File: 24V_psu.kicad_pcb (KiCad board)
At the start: 2 copper layers, 92.5 x 45 mm, 27 parts, among them J1 AC_IN, J2 DC_OUT, Q1 TIP122, Q2 BC546B

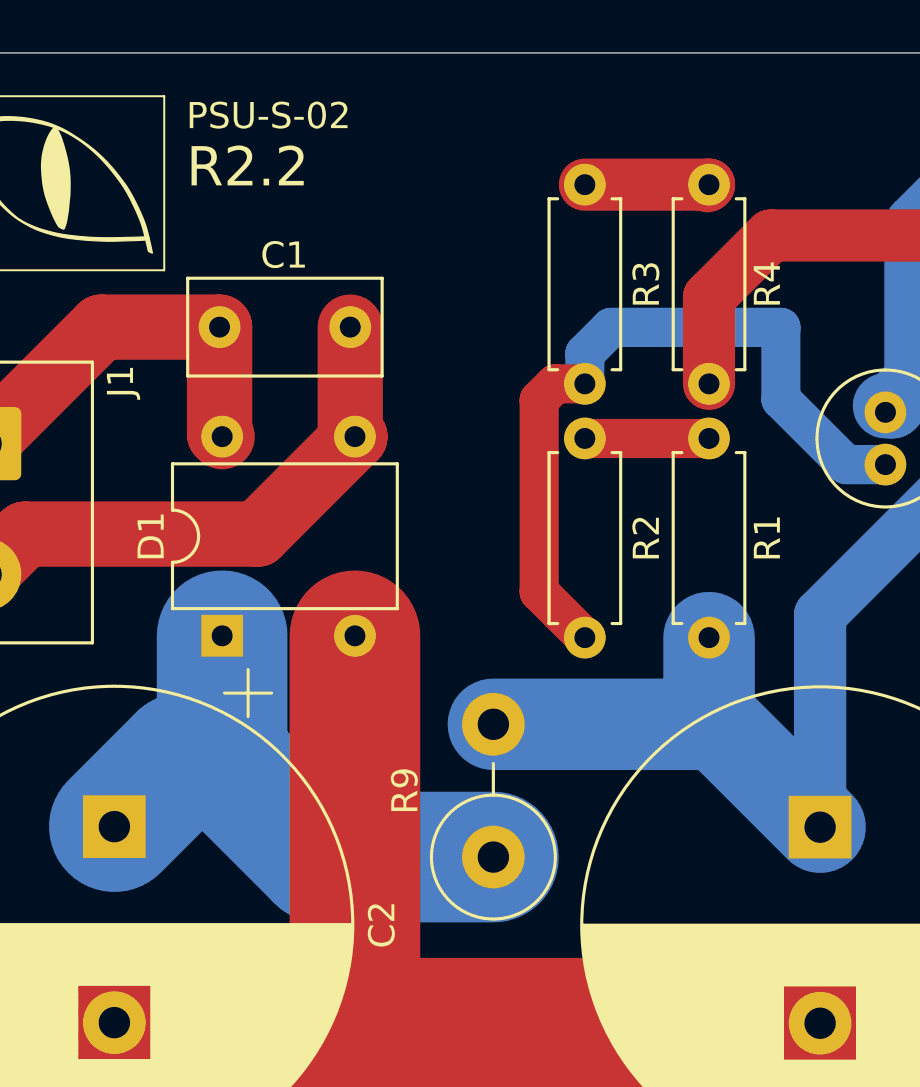
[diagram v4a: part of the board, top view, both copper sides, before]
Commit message: Rotate R9 around
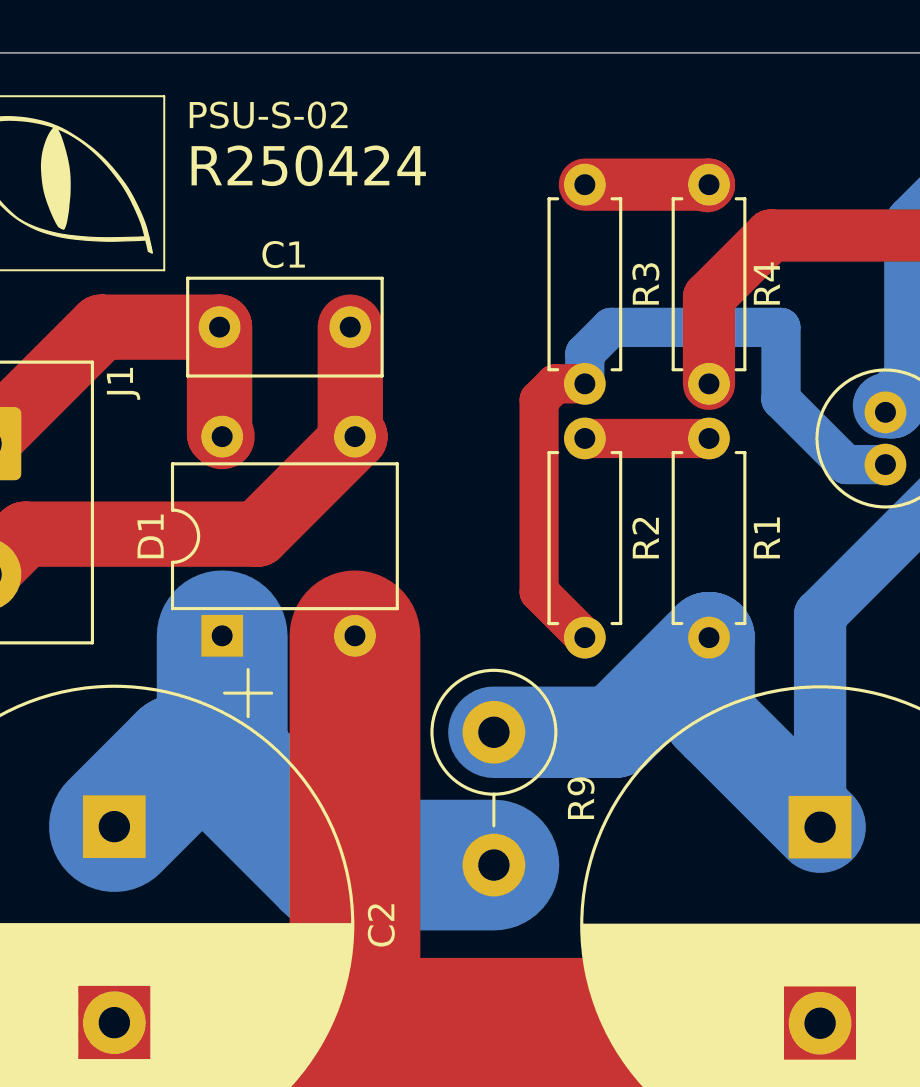
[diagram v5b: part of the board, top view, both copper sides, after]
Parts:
- moved R9 4.78 mm to (178.5, 73.5), turned to -90 degrees
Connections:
- R9 pad 1: Net-(D1-+) -> Net-(Q1-C)
- R9 pad 2: Net-(Q1-C) -> Net-(D1-+)
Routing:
- net Net-(Q1-C): track 44.7 -> 45.8 mm
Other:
- board text added: "R250424"
- board text removed: "R2.2"
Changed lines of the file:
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@@
 	(footprint "Resistor_THT:R_Axial_DIN0414_L11.9mm_D4.5mm_P5.08mm_Vertical"
 		(layer "F.Cu")
-		(at 178.5 78.265 90)
+		(at 178.52 73.49 -90)
 		(descr "Resistor, Axial_DIN0414 series, Axial, Vertical, pin pitch=5.08mm, 2W, length*diameter=11.9*4.5mm^2, http://www.vishay.com/docs/20128/wkxwrx.pdf")
 		(tags "Resistor Axial_DIN0414 series Axial Vertical pin pitch 5.08mm 2W length 11.9mm diameter 4.5mm")
@@
 		)
 		(property "Datasheet" ""
-			(at 0 0 90)
+			(at 0 0 270)
 			(unlocked yes)
 			(layer "F.Fab")
@@
 		)
 		(property "Description" "Resistor"
-			(at 0 0 90)
+			(at 0 0 270)
 			(unlocked yes)
 			(layer "F.Fab")
@@
 		)
 		(fp_line
-			(start 6.53 -2.5)
-			(end -2.5 -2.5)
+			(start -2.5 2.5)
+			(end 6.53 2.5)
 			(stroke
 				(width 0.05)
@@
 		)
 		(fp_line
-			(start -2.5 -2.5)
-			(end -2.5 2.5)
+			(start 6.53 2.5)
+			(end 6.53 -2.5)
 			(stroke
 				(width 0.05)
@@
 		)
 		(fp_line
-			(start 6.53 2.5)
-			(end 6.53 -2.5)
+			(start -2.5 -2.5)
+			(end -2.5 2.5)
 			(stroke
 				(width 0.05)
@@
 		)
 		(fp_line
-			(start -2.5 2.5)
-			(end 6.53 2.5)
+			(start 6.53 -2.5)
+			(end -2.5 -2.5)
 			(stroke
 				(width 0.05)
@@
 		)
 		(pad "1" thru_hole circle
-			(at 0 0 90)
+			(at 0 0 270)
 			(size 2.4 2.4)
 			(drill 1.2)
 			(layers "*.Cu" "*.Mask")
 			(remove_unused_layers no)
-			(net 3 "Net-(D1-+)")
+			(net 13 "Net-(Q1-C)")
 			(pintype "passive")
 		)
 		(pad "2" thru_hole oval
-			(at 5.08 0 90)
+			(at 5.08 0 270)
 			(size 2.4 2.4)
 			(drill 1.2)
 			(layers "*.Cu" "*.Mask")
 			(remove_unused_layers no)
-			(net 13 "Net-(Q1-C)")
+			(net 3 "Net-(D1-+)")
 			(pintype "passive")
 		)
@@
 		)
 	)
-	(gr_text "R2.2"
+	(gr_text "R250424"
 		(at 166.75 52.75 0)
 		(layer "F.SilkS")
@@
 	)
 	(segment
-		(start 171.891156 78.265)
-		(end 178.5 78.265)
+		(start 168.124188 74.498032)
+		(end 172.196156 78.57)
 		(width 5)
 		(layer "B.Cu")
@@
 	)
 	(segment
-		(start 168.124188 74.498032)
-		(end 166.601968 74.498032)
+		(start 172.196156 78.57)
+		(end 178.52 78.57)
 		(width 5)
 		(layer "B.Cu")
@@
 	(segment
 		(start 168.124188 74.498032)
-		(end 171.891156 78.265)
+		(end 166.601968 74.498032)
 		(width 5)
 		(layer "B.Cu")
@@
 	)
 	(segment
+		(start 183.13 73.49)
+		(end 178.52 73.49)
+		(width 3.5)
+		(layer "B.Cu")
+		(net 13)
+	)
+	(segment
 		(start 191 77.12222)
 		(end 191 69)
@@
 	)
 	(segment
-		(start 178.5 73.185)
-		(end 187.06278 73.185)
+		(start 187.06278 73.185)
+		(end 191 77.12222)
 		(width 3.5)
 		(layer "B.Cu")
@@
 	)
 	(segment
-		(start 187.06278 73.185)
-		(end 191 77.12222)
+		(start 186.75 69.87)
+		(end 183.13 73.49)
 		(width 3.5)
 		(layer "B.Cu")
@@
 	)
 	(group ""
-		(members "e9ad10b2-7d5c-4e9c-9937-1661a8a48dcf" "f2c60f9c-6234-4306-9854-33b4cfb3092c"
-			"fc57d3f7-0cdc-4cbc-a943-f06b294e3fd0"
-		)
-	)
-	(group ""
-		(members "082b185e-cb6b-406f-8bfc-4cf1e8c1ed41" "1c3a10e5-ed6b-4706-92ea-b0e31964ca46"
-			"2f4af1cf-109f-45bf-b2ad-1c70364eda2c" "36ea1de6-a0bc-4b95-9c79-2c91c7294a2a"
-			"3b4589bd-4bc9-4e1e-83e4-72cc03c78586" "485f2efe-d484-4d5a-b0cc-59a74a5c47fe"
-			"70c5d67f-a607-4099-a8f4-8ea4501b494e" "71ad5395-d93b-455e-b43b-2ba138f8bf88"
-			"aa8b4c11-b291-4553-bc7b-a7872eb0ac40" "e08a6ba4-3848-41e4-82e9-2b0b2aaaa8c0"
-		)
+		(members "e9ad10b2-7d5c-4e9c-9937-1661a8a48dcf" "fc57d3f7-0cdc-4cbc-a943-f06b294e3fd0")
 	)
 	(embedded_fonts no)
